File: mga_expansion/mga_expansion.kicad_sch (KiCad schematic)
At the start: 0 parts

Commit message: connect ISA address and data lines
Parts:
- added J1: Bus_ISA_8bit, symbol Connector:Bus_ISA_8bit
- added R1, R2, R3, R4, R5, R6, R7, R8: 330, symbol Device:R_Small
- added U1: W86855AF, Package_QFP:PQFP-100_14x20mm_P0.65mm, symbol Winbond:W86855AF
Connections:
- new net: J1.33 (DB7), R8.2
- new net: J1.34 (DB6), R7.2
- new net: J1.35 (DB5), R6.2
- new net: J1.36 (DB4), R5.2
- new net: J1.37 (DB3), R4.2
- new net: J1.38 (DB2), R3.2
- new net: J1.39 (DB1), R2.2
- new net: J1.40 (DB0), R1.2
- new net BA0: J1.62 (BA00), U1.1
- new net BA1: J1.61 (BA01), U1.2
- new net BA10: J1.52 (BA10), U1.11
- new net BA11: J1.51 (BA11), U1.12
- new net BA12: J1.50 (BA12), U1.13
- new net BA13: J1.49 (BA13), U1.14
- new net BA14: J1.48 (BA14), U1.15
- new net BA15: J1.47 (BA15), U1.16
- new net BA16: J1.46 (BA16), U1.17
- new net BA17: J1.45 (BA17), U1.18
- new net BA18: J1.44 (BA18), U1.19
- new net BA19: J1.43 (BA19), U1.20
- new net BA2: J1.60 (BA02), U1.3
- new net BA3: J1.59 (BA03), U1.4
- new net BA4: J1.58 (BA04), U1.5
- new net BA5: J1.57 (BA05), U1.6
- new net BA6: J1.56 (BA06), U1.7
- new net BA7: J1.55 (BA07), U1.8
- new net BA8: J1.54 (BA08), U1.9
- new net BA9: J1.53 (BA09), U1.10
- new net DB0: R1.1, U1.21
- new net DB1: R2.1, U1.22
- new net DB2: R3.1, U1.23
- new net DB3: R4.1, U1.24
- new net DB4: R5.1, U1.25
- new net DB5: R6.1, U1.26
- new net DB6: R7.1, U1.27
- new net DB7: R8.1, U1.28

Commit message: assign footprints to ISA connector and resistors
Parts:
- J1: footprint (none) -> local:BUS_XT
- R1, R2, R3, R4, R5, R6, R7, R8: footprint (none) -> Resistor_THT:R_Axial_DIN0207_L6.3mm_D2.5mm_P10.16mm_Horizontal
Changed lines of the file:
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@@
 			)
 		)
-		(property "Footprint" ""
+		(property "Footprint" "local:BUS_XT"
 			(at 101.6 166.37 0)
 			(effects
@@
 			)
 		)
-		(property "Footprint" ""
+		(property "Footprint" "Resistor_THT:R_Axial_DIN0207_L6.3mm_D2.5mm_P10.16mm_Horizontal"
 			(at 137.16 135.89 0)
 			(effects
@@
 			)
 		)
-		(property "Footprint" ""
+		(property "Footprint" "Resistor_THT:R_Axial_DIN0207_L6.3mm_D2.5mm_P10.16mm_Horizontal"
 			(at 124.46 142.24 0)
 			(effects
@@
 			)
 		)
-		(property "Footprint" ""
+		(property "Footprint" "Resistor_THT:R_Axial_DIN0207_L6.3mm_D2.5mm_P10.16mm_Horizontal"
 			(at 127 140.97 0)
 			(effects
@@
 			)
 		)
-		(property "Footprint" ""
+		(property "Footprint" "Resistor_THT:R_Axial_DIN0207_L6.3mm_D2.5mm_P10.16mm_Horizontal"
 			(at 134.62 137.16 0)
 			(effects
@@
 			)
 		)
-		(property "Footprint" ""
+		(property "Footprint" "Resistor_THT:R_Axial_DIN0207_L6.3mm_D2.5mm_P10.16mm_Horizontal"
 			(at 132.08 138.43 0)
 			(effects
@@
 			)
 		)
-		(property "Footprint" ""
+		(property "Footprint" "Resistor_THT:R_Axial_DIN0207_L6.3mm_D2.5mm_P10.16mm_Horizontal"
 			(at 121.92 143.51 0)
 			(effects
@@
 			)
 		)
-		(property "Footprint" ""
+		(property "Footprint" "Resistor_THT:R_Axial_DIN0207_L6.3mm_D2.5mm_P10.16mm_Horizontal"
 			(at 119.38 144.78 0)
 			(effects
@@
 			)
 		)
-		(property "Footprint" ""
+		(property "Footprint" "Resistor_THT:R_Axial_DIN0207_L6.3mm_D2.5mm_P10.16mm_Horizontal"
 			(at 129.54 139.7 0)
 			(effects

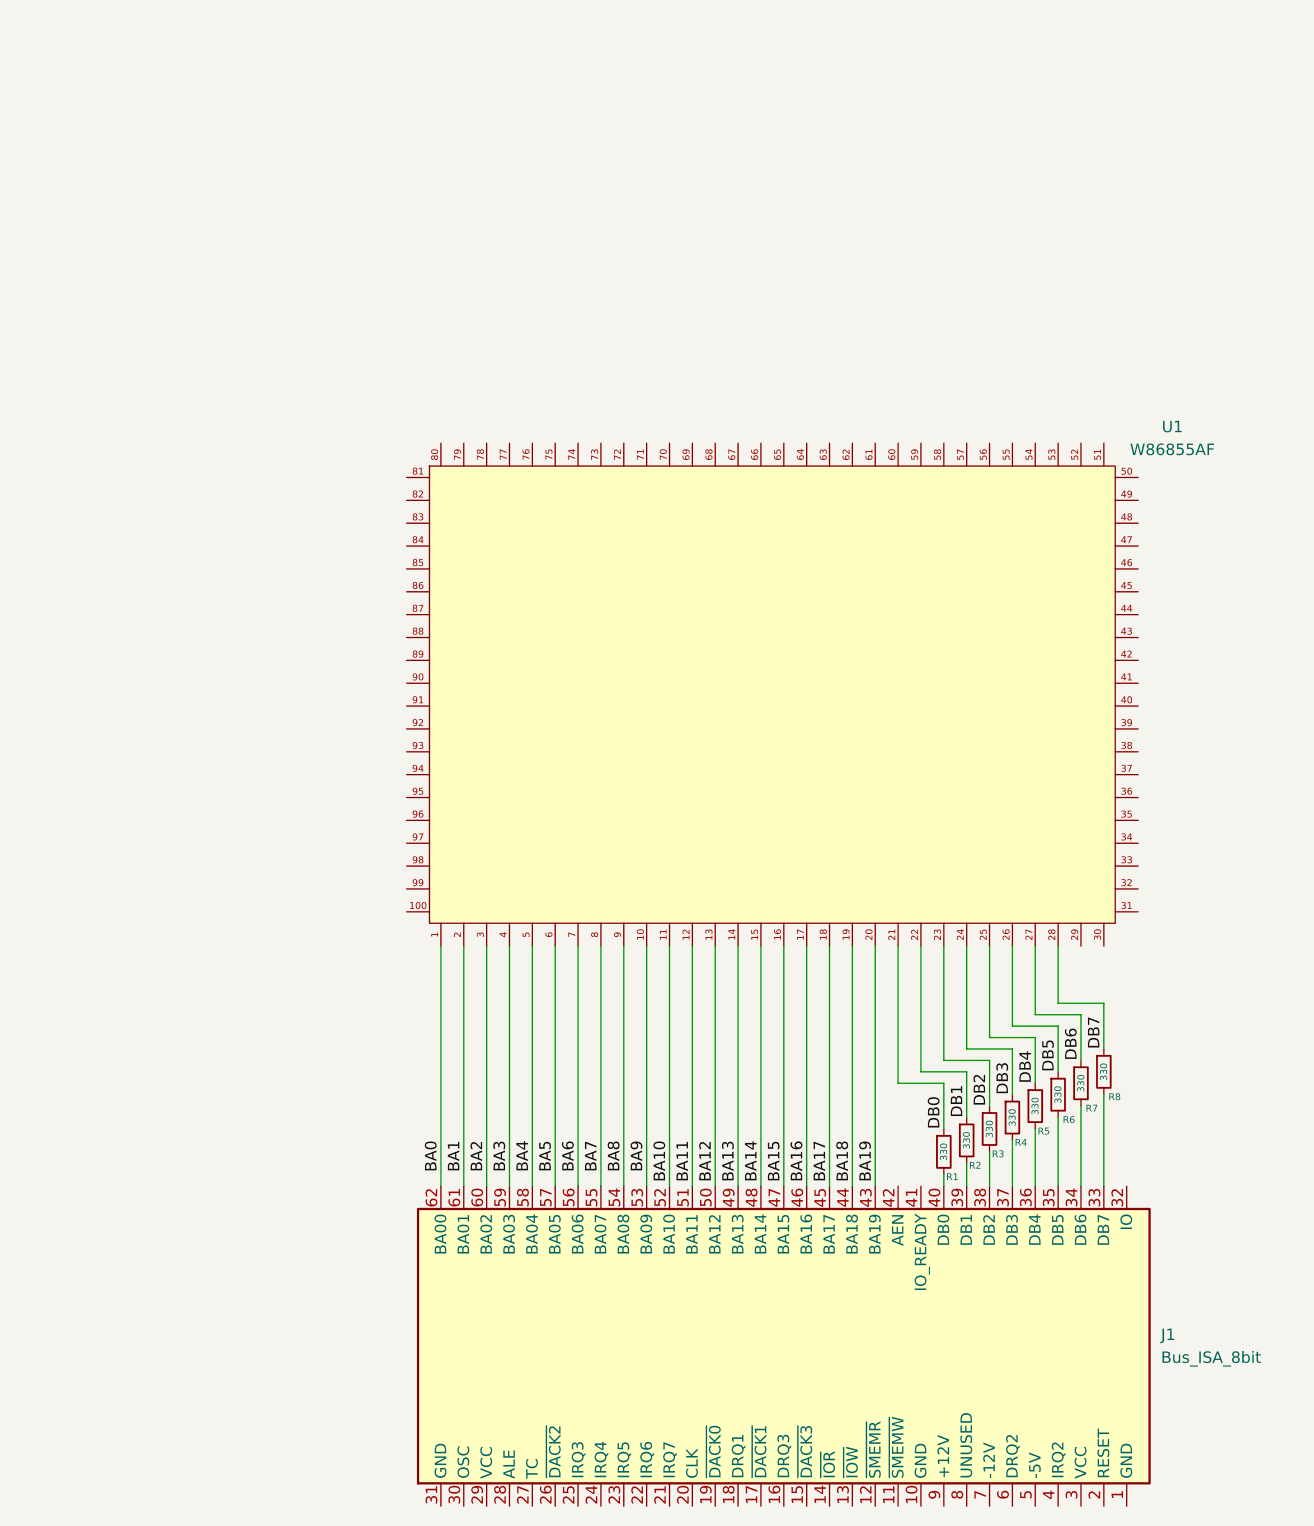
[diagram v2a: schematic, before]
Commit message: add RAM and ROM chips
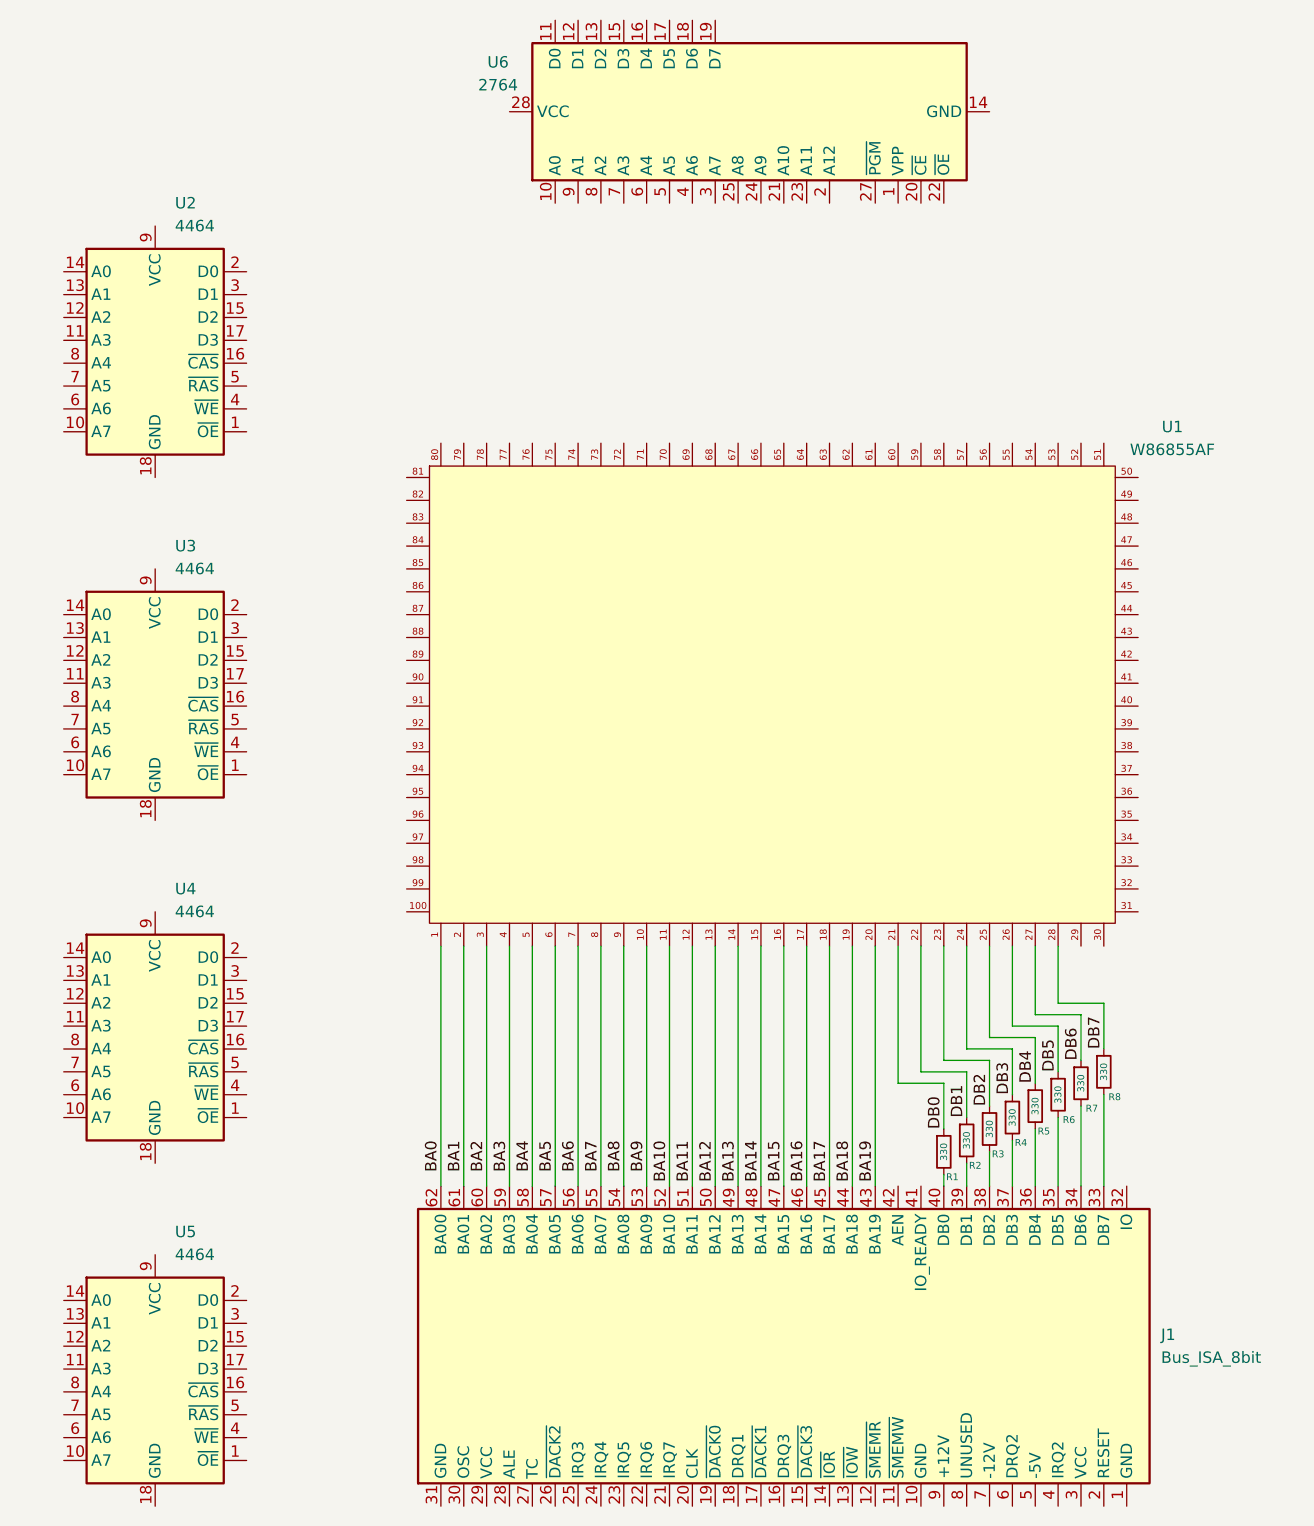
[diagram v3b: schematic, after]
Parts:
- added U2, U3, U4, U5: 4464, symbol Memory_Retro:4464
- added U6: 2764, Package_DIP:DIP-28_W15.24mm, symbol Memory_EPROM:2764

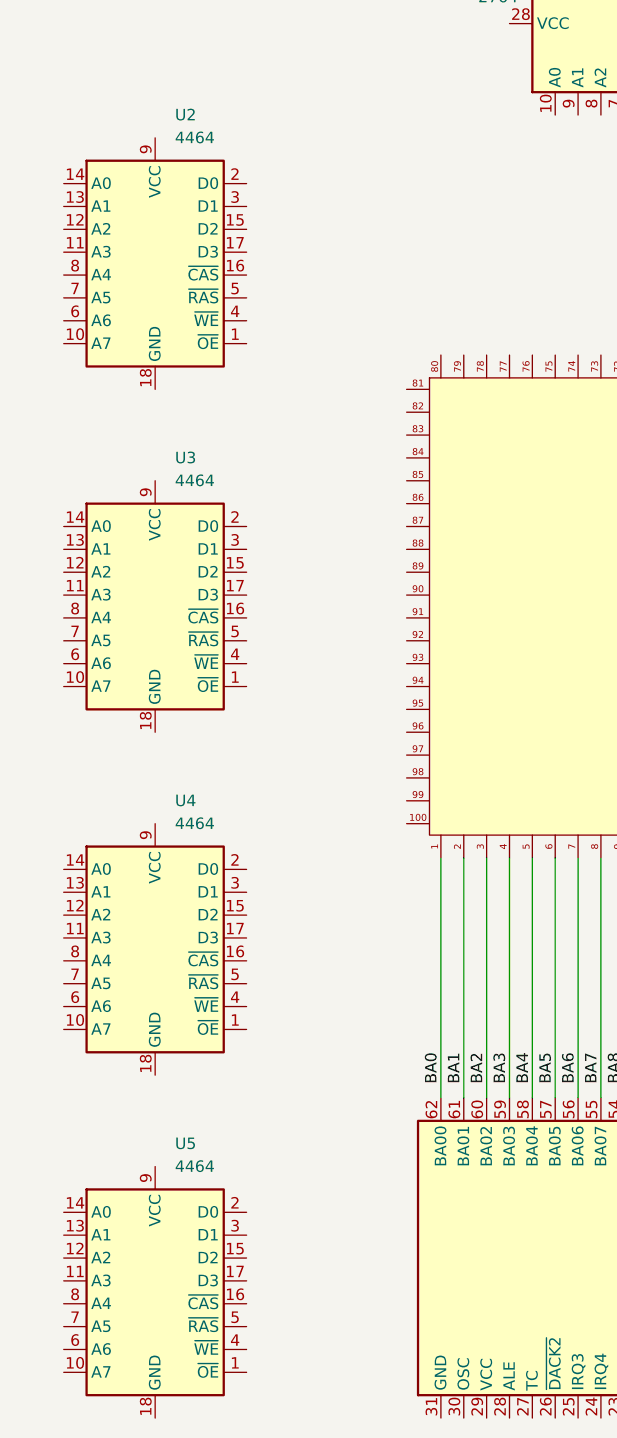
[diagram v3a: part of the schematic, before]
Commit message: trace RAM pinout according to memory datasheet
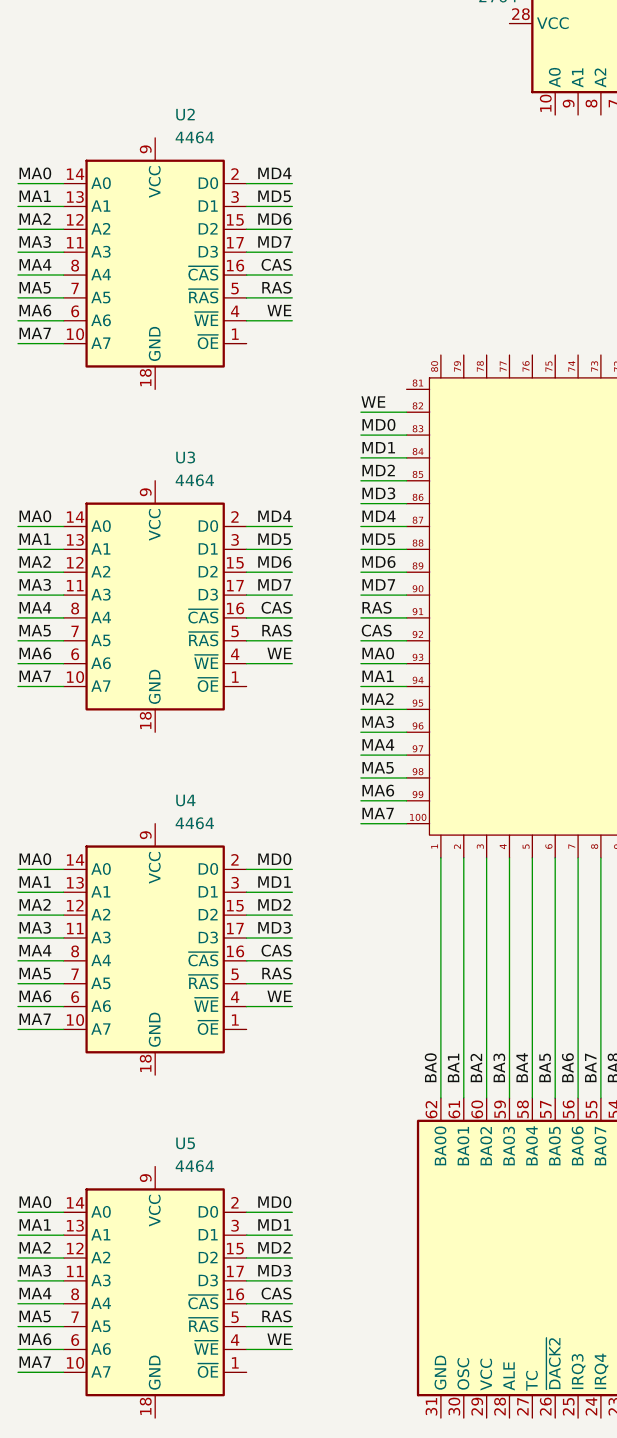
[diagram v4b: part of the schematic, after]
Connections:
- net MA7: now reaches U1.100
- net MA7: now also U2.10 (A7), U3.10 (A7), U4.10 (A7), U5.10 (A7)
- net WE: now reaches U1.82
- net WE: now also U2.4 (~{WE}), U3.4 (~{WE}), U4.4 (~{WE}), U5.4 (~{WE})
- net MD0: now reaches U1.83
- net MD0: now also U4.2 (D0), U5.2 (D0)
- net MD1: now reaches U1.84
- net MD1: now also U4.3 (D1), U5.3 (D1)
- net MD2: now reaches U1.85
- net MD2: now also U4.15 (D2), U5.15 (D2)
- net MD3: now reaches U1.86
- net MD3: now also U4.17 (D3), U5.17 (D3)
- net MD4: now reaches U1.87
- net MD4: now also U2.2 (D0), U3.2 (D0)
- net MD5: now reaches U1.88
- net MD5: now also U2.3 (D1), U3.3 (D1)
- net MD6: now reaches U1.89
- net MD6: now also U2.15 (D2), U3.15 (D2)
- net MD7: now reaches U1.90
- net MD7: now also U2.17 (D3), U3.17 (D3)
- net RAS: now reaches U1.91
- net RAS: now also U2.5 (~{RAS}), U3.5 (~{RAS}), U4.5 (~{RAS}), U5.5 (~{RAS})
- net CAS: now reaches U1.92
- net CAS: now also U2.16 (~{CAS}), U3.16 (~{CAS}), U4.16 (~{CAS}), U5.16 (~{CAS})
- net MA0: now reaches U1.93
- net MA0: now also U2.14 (A0), U3.14 (A0), U4.14 (A0), U5.14 (A0)
- net MA1: now reaches U1.94
- net MA1: now also U2.13 (A1), U3.13 (A1), U4.13 (A1), U5.13 (A1)
- net MA2: now reaches U1.95
- net MA2: now also U2.12 (A2), U3.12 (A2), U4.12 (A2), U5.12 (A2)
- net MA3: now reaches U1.96
- net MA3: now also U2.11 (A3), U3.11 (A3), U4.11 (A3), U5.11 (A3)
- net MA4: now reaches U1.97
- net MA4: now also U2.8 (A4), U3.8 (A4), U4.8 (A4), U5.8 (A4)
- net MA5: now reaches U1.98
- net MA5: now also U2.7 (A5), U3.7 (A5), U4.7 (A5), U5.7 (A5)
- net MA6: now reaches U1.99
- net MA6: now also U2.6 (A6), U3.6 (A6), U4.6 (A6), U5.6 (A6)
